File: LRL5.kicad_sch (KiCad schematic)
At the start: 38 parts, among them J1 POWER, J2 On/Off, J5 OUT, J6 MODE, J7 ADJUST, Q1 BC549, U1 BA033CC0T, U2 NHD-C0220BIZ

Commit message: Fix some silkscreen overlaps
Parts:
- TP1, TP2: footprint TestPoint:TestPoint_Pad_2.5x2.5mm -> TestPoint:TestPoint_THTPad_2.0x2.0mm_Drill1.0mm
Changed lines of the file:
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@@
 			)
 		)
-		(property "Footprint" "TestPoint:TestPoint_Pad_2.5x2.5mm"
+		(property "Footprint" "TestPoint:TestPoint_THTPad_2.0x2.0mm_Drill1.0mm"
 			(at 179.07 148.59 0)
 			(effects
@@
 			)
 		)
-		(property "Footprint" "TestPoint:TestPoint_Pad_2.5x2.5mm"
+		(property "Footprint" "TestPoint:TestPoint_THTPad_2.0x2.0mm_Drill1.0mm"
 			(at 189.23 123.19 0)
 			(effects

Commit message: Some PCB optimizations 1
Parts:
- removed R10, R11, R12, R13, R14, R9: 10k, Resistor_SMD:R_0805_2012Metric_Pad1.20x1.40mm_HandSolder, symbol Device:R
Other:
- moved on the sheet: C4, C5, C6, J7, R6, R7, U2

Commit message: Redesign board for smaller size
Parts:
- H1, H2, H3, H4: footprint MountingHole:MountingHole_3.2mm_M3 -> MountingHole:MountingHole_2.5mm
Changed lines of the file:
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@@
 			)
 		)
-		(property "Footprint" "MountingHole:MountingHole_3.2mm_M3"
+		(property "Footprint" "MountingHole:MountingHole_2.5mm"
 			(at 25.4 104.14 0)
 			(effects
@@
 			)
 		)
-		(property "Footprint" "MountingHole:MountingHole_3.2mm_M3"
+		(property "Footprint" "MountingHole:MountingHole_2.5mm"
 			(at 25.4 109.22 0)
 			(effects
@@
 			)
 		)
-		(property "Footprint" "MountingHole:MountingHole_3.2mm_M3"
+		(property "Footprint" "MountingHole:MountingHole_2.5mm"
 			(at 25.4 99.06 0)
 			(effects
@@
 			)
 		)
-		(property "Footprint" "MountingHole:MountingHole_3.2mm_M3"
+		(property "Footprint" "MountingHole:MountingHole_2.5mm"
 			(at 25.4 93.98 0)
 			(effects

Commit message: Change diodes footprints
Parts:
- D1: footprint Diode_THT:D_DO-41_SOD81_P10.16mm_Horizontal -> Diode_SMD:D_SMA_Handsoldering
- D2: footprint Diode_THT:D_DO-35_SOD27_P7.62mm_Horizontal -> Diode_SMD:D_SMA_Handsoldering
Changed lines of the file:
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@@
 			)
 		)
-		(property "Footprint" "Diode_THT:D_DO-35_SOD27_P7.62mm_Horizontal"
+		(property "Footprint" "Diode_SMD:D_SMA_Handsoldering"
 			(at 50.8 144.78 0)
 			(effects
@@
 			)
 		)
-		(property "Footprint" "Diode_THT:D_DO-41_SOD81_P10.16mm_Horizontal"
+		(property "Footprint" "Diode_SMD:D_SMA_Handsoldering"
 			(at 237.49 131.445 0)
 			(effects

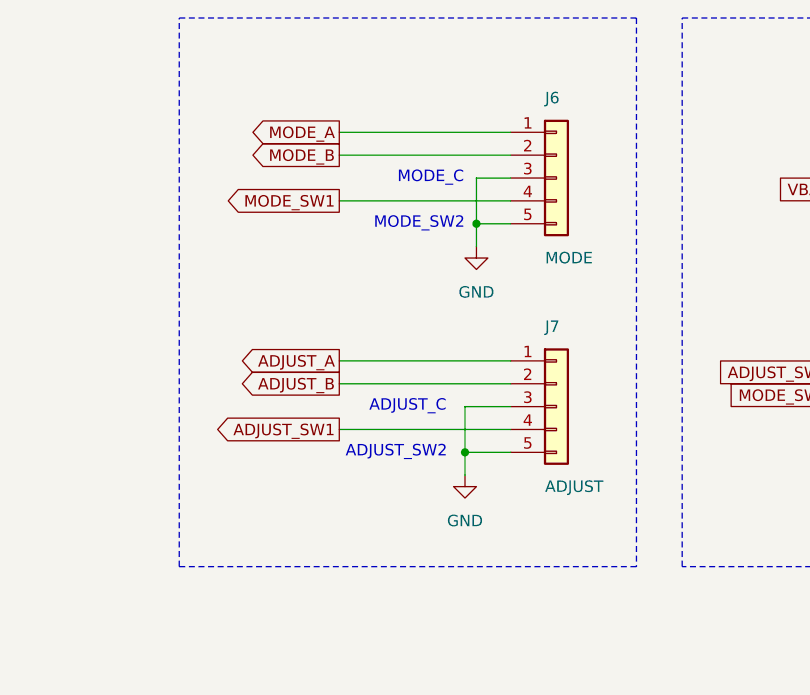
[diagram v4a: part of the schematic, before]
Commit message: Redesign board. Move connectors
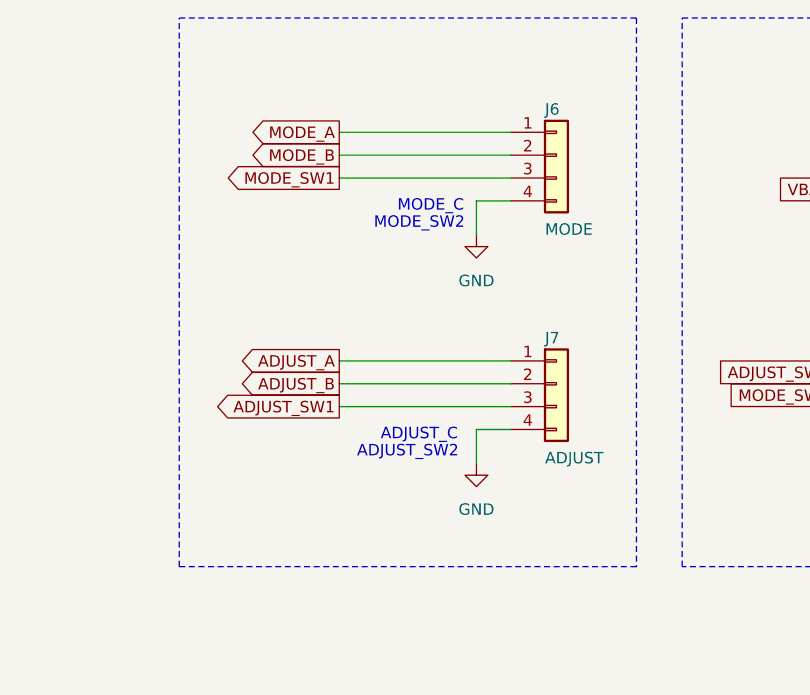
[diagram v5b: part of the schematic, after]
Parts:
- removed J6: MODE, Connector_PinHeader_2.54mm:PinHeader_1x05_P2.54mm_Vertical, symbol Connector_Generic:Conn_01x05
- removed J7: ADJUST, Connector_PinHeader_2.54mm:PinHeader_1x05_P2.54mm_Vertical, symbol Connector_Generic:Conn_01x05
- added J6: MODE, Connector_PinHeader_2.54mm:PinHeader_1x04_P2.54mm_Vertical, symbol Connector_Generic:Conn_01x04
- added J7: ADJUST, Connector_PinHeader_2.54mm:PinHeader_1x04_P2.54mm_Vertical, symbol Connector_Generic:Conn_01x04
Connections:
- net ADJUST_A: now also J7.1 (Pin_1)
- net ADJUST_B: now also J7.2 (Pin_2)
- net ADJUST_SW1: now also J7.3 (Pin_3)
- net GND: now also J6.4 (Pin_4), J7.4 (Pin_4)
- net MODE_A: now also J6.1 (Pin_1)
- net MODE_B: now also J6.2 (Pin_2)
- net MODE_SW1: now also J6.3 (Pin_3)

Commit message: Change some pins so thay don't interact with JTAG
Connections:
- net ADJUST_B: now also J3.13 (Pin_13); no longer J3.10 (Pin_10)
- net FOUT: now also J4.16 (Pin_16); no longer J3.11 (Pin_11)
- net MODE_B: now also J3.12 (Pin_12); no longer J3.9 (Pin_9)
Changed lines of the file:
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@@
+	)
+	(no_connect
+		(at 255.27 57.15)
 	)
 	(no_connect
@@
 	)
 	(no_connect
-		(at 255.27 64.77)
-	)
-	(no_connect
 		(at 255.27 77.47)
 	)
@@
 	)
 	(no_connect
-		(at 255.27 62.23)
-	)
-	(no_connect
 		(at 255.27 82.55)
 	)
@@
 	)
 	(no_connect
+		(at 255.27 54.61)
+	)
+	(no_connect
+		(at 226.06 57.15)
+	)
+	(no_connect
 		(at 226.06 46.99)
 	)
 	(no_connect
-		(at 226.06 57.15)
-	)
-	(no_connect
-		(at 226.06 72.39)
-	)
-	(no_connect
 		(at 255.27 67.31)
 	)
@@
 	)
 	(no_connect
+		(at 255.27 59.69)
+	)
+	(no_connect
 		(at 226.06 41.91)
 	)
@@
 	(wire
 		(pts
-			(xy 255.27 57.15) (xy 260.35 57.15)
-		)
-		(stroke
-			(width 0)
-			(type default)
-		)
-	)
-	(wire
-		(pts
 			(xy 259.08 137.16) (xy 254 137.16)
 		)
@@
 	(wire
 		(pts
+			(xy 220.98 72.39) (xy 226.06 72.39)
+		)
+		(stroke
+			(width 0)
+			(type default)
+		)
+	)
+	(wire
+		(pts
 			(xy 165.1 40.64) (xy 184.15 40.64)
 		)
@@
 	(wire
 		(pts
-			(xy 255.27 59.69) (xy 260.35 59.69)
+			(xy 255.27 64.77) (xy 260.35 64.77)
 		)
 		(stroke
@@
 	(wire
 		(pts
-			(xy 255.27 54.61) (xy 260.35 54.61)
+			(xy 255.27 62.23) (xy 260.35 62.23)
 		)
 		(stroke
@@
 	(global_label "ADJUST_B"
 		(shape input)
-		(at 260.35 57.15 0)
+		(at 260.35 64.77 0)
 		(fields_autoplaced yes)
 		(effects
@@
 		)
 		(property "Intersheetrefs" "${INTERSHEET_REFS}"
-			(at 272.4066 57.15 0)
+			(at 272.4066 64.77 0)
 			(effects
 				(font
@@
 	(global_label "MODE_B"
 		(shape input)
-		(at 260.35 54.61 0)
+		(at 260.35 62.23 0)
 		(fields_autoplaced yes)
 		(effects
@@
 		)
 		(property "Intersheetrefs" "${INTERSHEET_REFS}"
-			(at 270.7737 54.61 0)
+			(at 270.7737 62.23 0)
 			(effects
 				(font
@@
 	(global_label "FOUT"
 		(shape output)
-		(at 260.35 59.69 0)
-		(fields_autoplaced yes)
-		(effects
-			(font
-				(size 1.27 1.27)
-			)
-			(justify left)
-		)
-		(property "Intersheetrefs" "${INTERSHEET_REFS}"
-			(at 268.0524 59.69 0)
-			(effects
-				(font
-					(size 1.27 1.27)
-				)
-				(justify left)
-				(hide yes)
-			)
+		(at 220.98 72.39 180)
+		(fields_autoplaced yes)
+		(effects
+			(font
+				(size 1.27 1.27)
+			)
+			(justify right)
+		)
+		(property "Intersheetrefs" "${INTERSHEET_REFS}"
+			(at 213.2776 72.39 0)
+			(effects
+				(font
+					(size 1.27 1.27)
+				)
+				(justify right)
+				(hide yes)
+			)

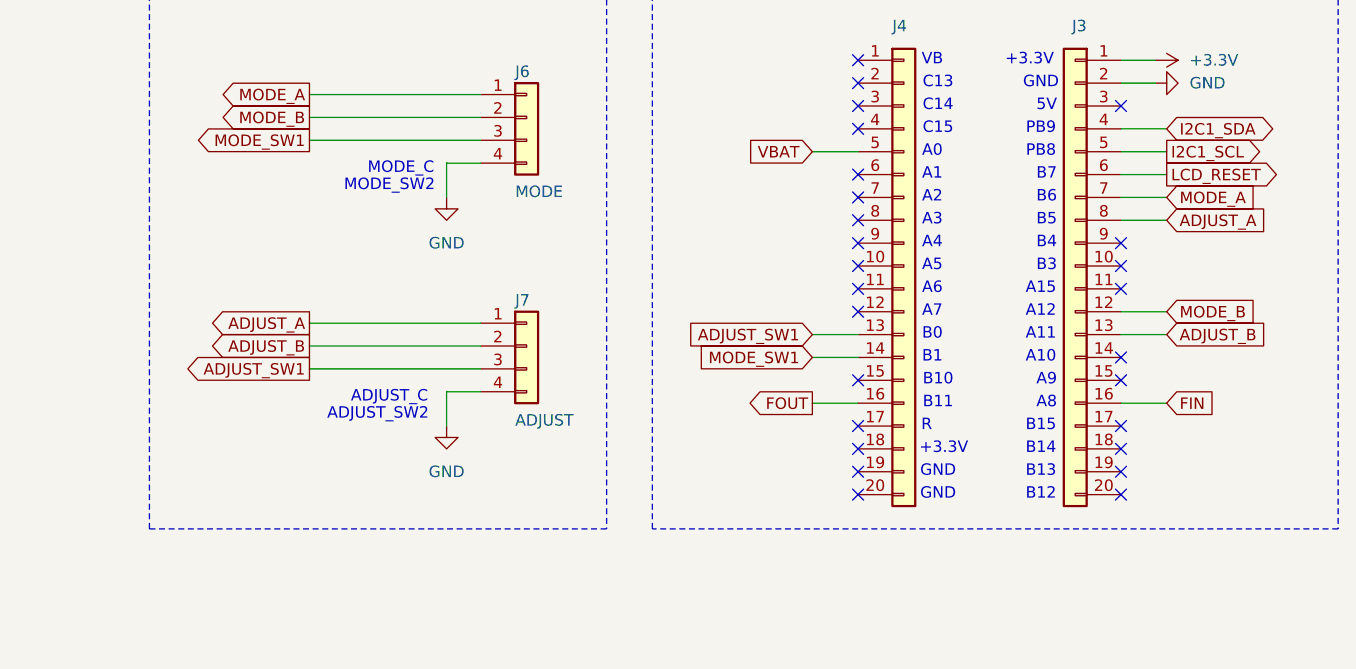
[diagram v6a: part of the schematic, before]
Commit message: Remove ADJUST connector
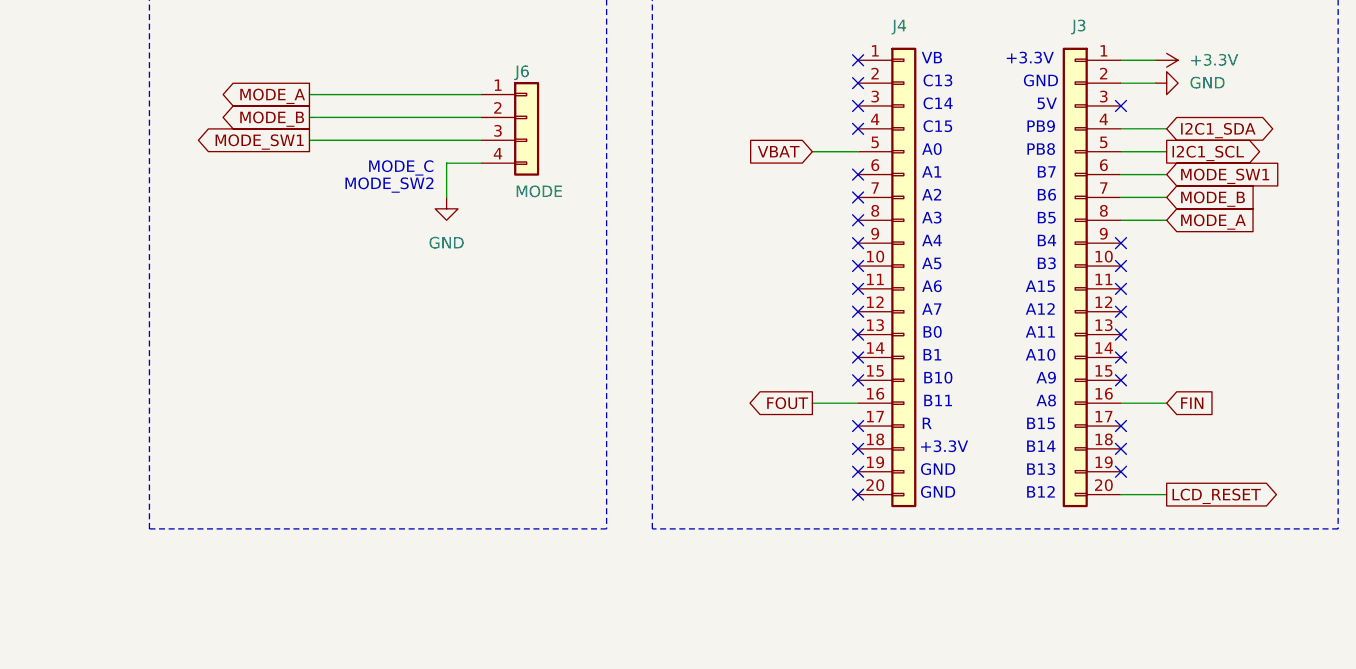
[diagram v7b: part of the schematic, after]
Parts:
- removed J7: ADJUST, Connector_PinHeader_2.54mm:PinHeader_1x04_P2.54mm_Vertical, symbol Connector_Generic:Conn_01x04
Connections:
- net ADJUST_A is gone; now on net MODE_A: J3.8 (Pin_8)
- net LCD_RESET: now also J3.20 (Pin_20); no longer J3.6 (Pin_6)
- net MODE_A: no longer J3.7 (Pin_7)
- net MODE_B: now also J3.7 (Pin_7); no longer J3.12 (Pin_12)
- net MODE_SW1: now also J3.6 (Pin_6); no longer J4.14 (Pin_14)
- net ADJUST_B: no longer names the net of J3.13 (Pin_13)
- net ADJUST_SW1: no longer names the net of J4.13 (Pin_13)
- no-connect marks 26 -> 29
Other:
- note removed: "ADJUST_C"
- note removed: "ADJUST_SW2"

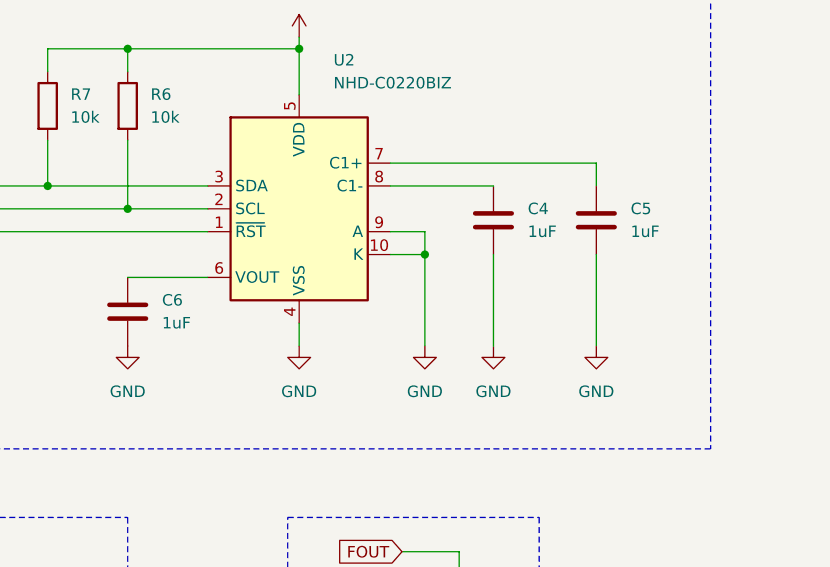
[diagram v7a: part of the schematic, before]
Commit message: Fix LCD capacitor
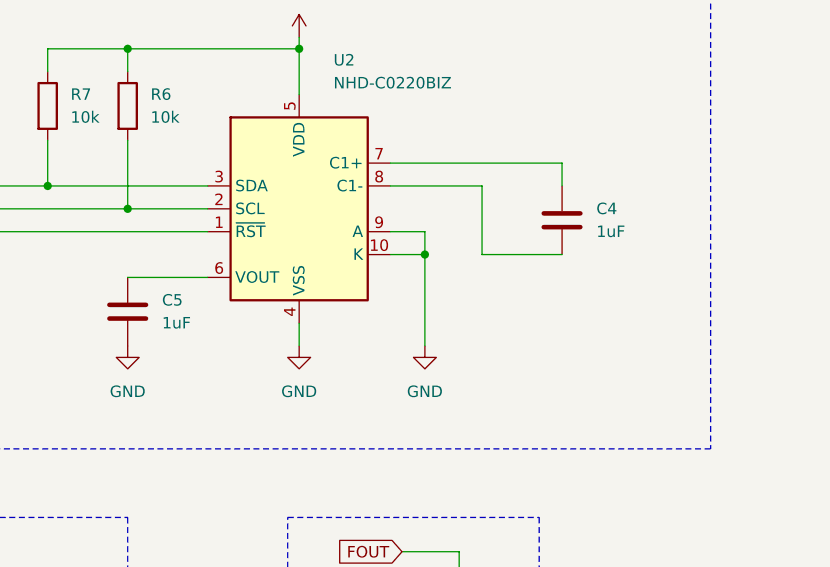
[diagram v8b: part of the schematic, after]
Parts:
- removed C5: 1uF, Capacitor_SMD:C_0805_2012Metric_Pad1.18x1.45mm_HandSolder, symbol Device:C
- renumbered C6 to C5
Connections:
- net GND: no longer C4.2
- net at U2.7 (C1+): now also C4.1
- net at U2.8 (C1-): now also C4.2; no longer C4.1
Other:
- moved on the sheet: C4
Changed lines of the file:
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@@
 	(wire
 		(pts
+			(xy 92.71 59.69) (xy 101.6 59.69)
+		)
+		(stroke
+			(width 0)
+			(type default)
+		)
+	)
+	(wire
+		(pts
 			(xy 90.17 105.41) (xy 90.17 102.87)
 		)
@@
 	(wire
 		(pts
-			(xy 82.55 52.07) (xy 93.98 52.07)
-		)
-		(stroke
-			(width 0)
-			(type default)
-		)
-	)
-	(wire
-		(pts
 			(xy 72.39 36.83) (xy 53.34 36.83)
 		)
@@
 	(wire
 		(pts
-			(xy 82.55 49.53) (xy 105.41 49.53)
+			(xy 86.36 149.86) (xy 86.36 170.18)
 		)
 		(stroke
@@
 	(wire
 		(pts
-			(xy 86.36 149.86) (xy 86.36 170.18)
+			(xy 101.6 49.53) (xy 101.6 52.07)
 		)
 		(stroke
@@
 	(wire
 		(pts
+			(xy 82.55 49.53) (xy 101.6 49.53)
+		)
+		(stroke
+			(width 0)
+			(type default)
+		)
+	)
+	(wire
+		(pts
 			(xy 255.27 46.99) (xy 260.35 46.99)
 		)
@@
 	(wire
 		(pts
+			(xy 92.71 52.07) (xy 92.71 59.69)
+		)
+		(stroke
+			(width 0)
+			(type default)
+		)
+	)
+	(wire
+		(pts
 			(xy 171.45 127) (xy 184.15 127)
 		)
@@
 	(wire
 		(pts
-			(xy 105.41 49.53) (xy 105.41 52.07)
+			(xy 36.83 52.07) (xy 44.45 52.07)
 		)
 		(stroke
@@
 	(wire
 		(pts
-			(xy 36.83 52.07) (xy 44.45 52.07)
+			(xy 184.15 127) (xy 184.15 132.08)
 		)
 		(stroke
@@
 	(wire
 		(pts
-			(xy 184.15 127) (xy 184.15 132.08)
+			(xy 165.1 38.1) (xy 184.15 38.1)
 		)
 		(stroke
@@
 	(wire
 		(pts
-			(xy 165.1 38.1) (xy 184.15 38.1)
+			(xy 83.82 92.71) (xy 90.17 92.71)
 		)
 		(stroke
@@
 	(wire
 		(pts
-			(xy 83.82 92.71) (xy 90.17 92.71)
+			(xy 82.55 52.07) (xy 92.71 52.07)
 		)
 		(stroke
@@
 	(wire
 		(pts
-			(xy 105.41 59.69) (xy 105.41 69.85)
-		)
-		(stroke
-			(width 0)
-			(type default)
-		)
-	)
-	(wire
-		(pts
-			(xy 93.98 59.69) (xy 93.98 69.85)
-		)
-		(stroke
-			(width 0)
-			(type default)
-		)
-	)
-	(wire
-		(pts
 			(xy 229.87 121.92) (xy 229.87 127)
 		)
@@
 	)
 	(symbol
-		(lib_id "Device:C")
-		(at 105.41 55.88 0)
-		(unit 1)
-		(exclude_from_sim no)
-		(in_bom yes)
-		(on_board yes)
-		(dnp no)
-		(fields_autoplaced yes)
-		(property "Reference" "C5"
-			(at 109.22 54.6099 0)
-			(effects
-				(font
-					(size 1.27 1.27)
-				)
-				(justify left)
-			)
-		)
-		(property "Value" "1uF"
-			(at 109.22 57.1499 0)
-			(effects
-				(font
-					(size 1.27 1.27)
-				)
-				(justify left)
-			)
-		)
-		(property "Footprint" "Capacitor_SMD:C_0805_2012Metric_Pad1.18x1.45mm_HandSolder"
-			(at 106.3752 59.69 0)
-			(effects
-				(font
-					(size 1.27 1.27)
-				)
-				(hide yes)
-			)
-		)
-		(property "Datasheet" "~"
-			(at 105.41 55.88 0)
-			(effects
-				(font
-					(size 1.27 1.27)
-				)
-				(hide yes)
-			)
-		)
-		(property "Description" "Unpolarized capacitor"
-			(at 105.41 55.88 0)
-			(effects
-				(font
-					(size 1.27 1.27)
-				)
-				(hide yes)
-			)
-		)
-		(pin "1"
-		)
-		(pin "2"
-		)
-		(instances
-			(project ""
-				(path "/ffc94b8d-ae8a-4b9a-afc3-af60dc91e04f"
-					(reference "C5")
-					(unit 1)
-				)
-			)
-		)
-	)
-	(symbol
 		(lib_id "Device:R")
 		(at 59.69 137.16 0)
@@
 	)
 	(symbol
-		(lib_id "power:GND")
-		(at 93.98 69.85 0)
-		(unit 1)
-		(exclude_from_sim no)
-		(in_bom yes)
-		(on_board yes)
-		(dnp no)
-		(fields_autoplaced yes)
-		(property "Reference" "#PWR013"
-			(at 93.98 76.2 0)
-			(effects
-				(font
-					(size 1.27 1.27)
-				)
-				(hide yes)
-			)
-		)
-		(property "Value" "GND"
-			(at 93.98 74.93 0)
-			(effects
-				(font
-					(size 1.27 1.27)
-				)
-			)
-		)
-		(property "Footprint" ""
-			(at 93.98 69.85 0)
-			(effects
-				(font
-					(size 1.27 1.27)
-				)
-				(hide yes)
-			)
-		)
-		(property "Datasheet" ""
-			(at 93.98 69.85 0)
-			(effects
-				(font
-					(size 1.27 1.27)
-				)
-				(hide yes)
-			)
-		)
-		(property "Description" "Power symbol creates a global label with name \"GND\" , ground"
-			(at 93.98 69.85 0)
-			(effects
-				(font
-					(size 1.27 1.27)
-				)
-				(hide yes)
-			)
-		)
-		(pin "1"
-		)
-		(instances
-			(project ""
-				(path "/ffc94b8d-ae8a-4b9a-afc3-af60dc91e04f"
-					(reference "#PWR013")
-					(unit 1)
-				)
-			)
-		)
-	)
-	(symbol
 		(lib_id "Device:C")
 		(at 218.44 135.89 0)
@@
 		(dnp no)
 		(fields_autoplaced yes)
-		(property "Reference" "C6"
+		(property "Reference" "C5"
 			(at 57.15 64.7699 0)
 			(effects
@@
 			(project ""
 				(path "/ffc94b8d-ae8a-4b9a-afc3-af60dc91e04f"
-					(reference "C6")
-					(unit 1)
-				)
-			)
-		)
-	)
-	(symbol
-		(lib_id "power:GND")
-		(at 105.41 69.85 0)
-		(unit 1)
-		(exclude_from_sim no)
-		(in_bom yes)
-		(on_board yes)
-		(dnp no)
-		(fields_autoplaced yes)
-		(property "Reference" "#PWR014"
-			(at 105.41 76.2 0)
-			(effects
-				(font
-					(size 1.27 1.27)
-				)
-				(hide yes)
-			)
-		)
-		(property "Value" "GND"
-			(at 105.41 74.93 0)
-			(effects
-				(font
-					(size 1.27 1.27)
-				)
-			)
-		)
-		(property "Footprint" ""
-			(at 105.41 69.85 0)
-			(effects
-				(font
-					(size 1.27 1.27)
-				)
-				(hide yes)
-			)
-		)
-		(property "Datasheet" ""
-			(at 105.41 69.85 0)
-			(effects
-				(font
-					(size 1.27 1.27)
-				)
-				(hide yes)
-			)
-		)
-		(property "Description" "Power symbol creates a global label with name \"GND\" , ground"
-			(at 105.41 69.85 0)
-			(effects
-				(font
-					(size 1.27 1.27)
-				)
-				(hide yes)
-			)
-		)
-		(pin "1"
-		)
-		(instances
-			(project ""
-				(path "/ffc94b8d-ae8a-4b9a-afc3-af60dc91e04f"
-					(reference "#PWR014")
+					(reference "C5")
 					(unit 1)
 				)
@@
 	(symbol
 		(lib_id "Device:C")
-		(at 93.98 55.88 0)
+		(at 101.6 55.88 0)
 		(unit 1)
 		(exclude_from_sim no)
@@
 		(fields_autoplaced yes)
 		(property "Reference" "C4"
-			(at 97.79 54.6099 0)
+			(at 105.41 54.6099 0)
 			(effects
 				(font
@@
 		)
 		(property "Value" "1uF"
-			(at 97.79 57.1499 0)
+			(at 105.41 57.1499 0)
 			(effects
 				(font
@@
 		)
 		(property "Footprint" "Capacitor_SMD:C_0805_2012Metric_Pad1.18x1.45mm_HandSolder"
-			(at 94.9452 59.69 0)
+			(at 102.5652 59.69 0)
 			(effects
 				(font
@@
 		)
 		(property "Datasheet" "~"
-			(at 93.98 55.88 0)
+			(at 101.6 55.88 0)
 			(effects
 				(font
@@
 		)
 		(property "Description" "Unpolarized capacitor"
-			(at 93.98 55.88 0)
+			(at 101.6 55.88 0)
 			(effects
 				(font
